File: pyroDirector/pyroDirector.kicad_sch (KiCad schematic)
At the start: 37 parts, among them J1 AudioJack3.5mm, J10 Ext_Btn_Down, J11 Ext_Btn_Up, J12 Ext_Btn_Left, J13 Ext_Btn_Right, J14 Ext_Btn_OK, J15 PWR_CONN, J16 CALIB_MODULE, J17 DISP_I2C, J2 Header_A1-A15, J3 Header_D14-19, J4 Header_D48-53, J5 V_Batt, J6 Header_ISP, J7 PWR_SWITCH, J8 Batt, J9 Ext_Btn_Cncl, Q1 MMBT2222A 1P, SW1 EN_SW, U1 MEGA_PRO_ATMEGA2560

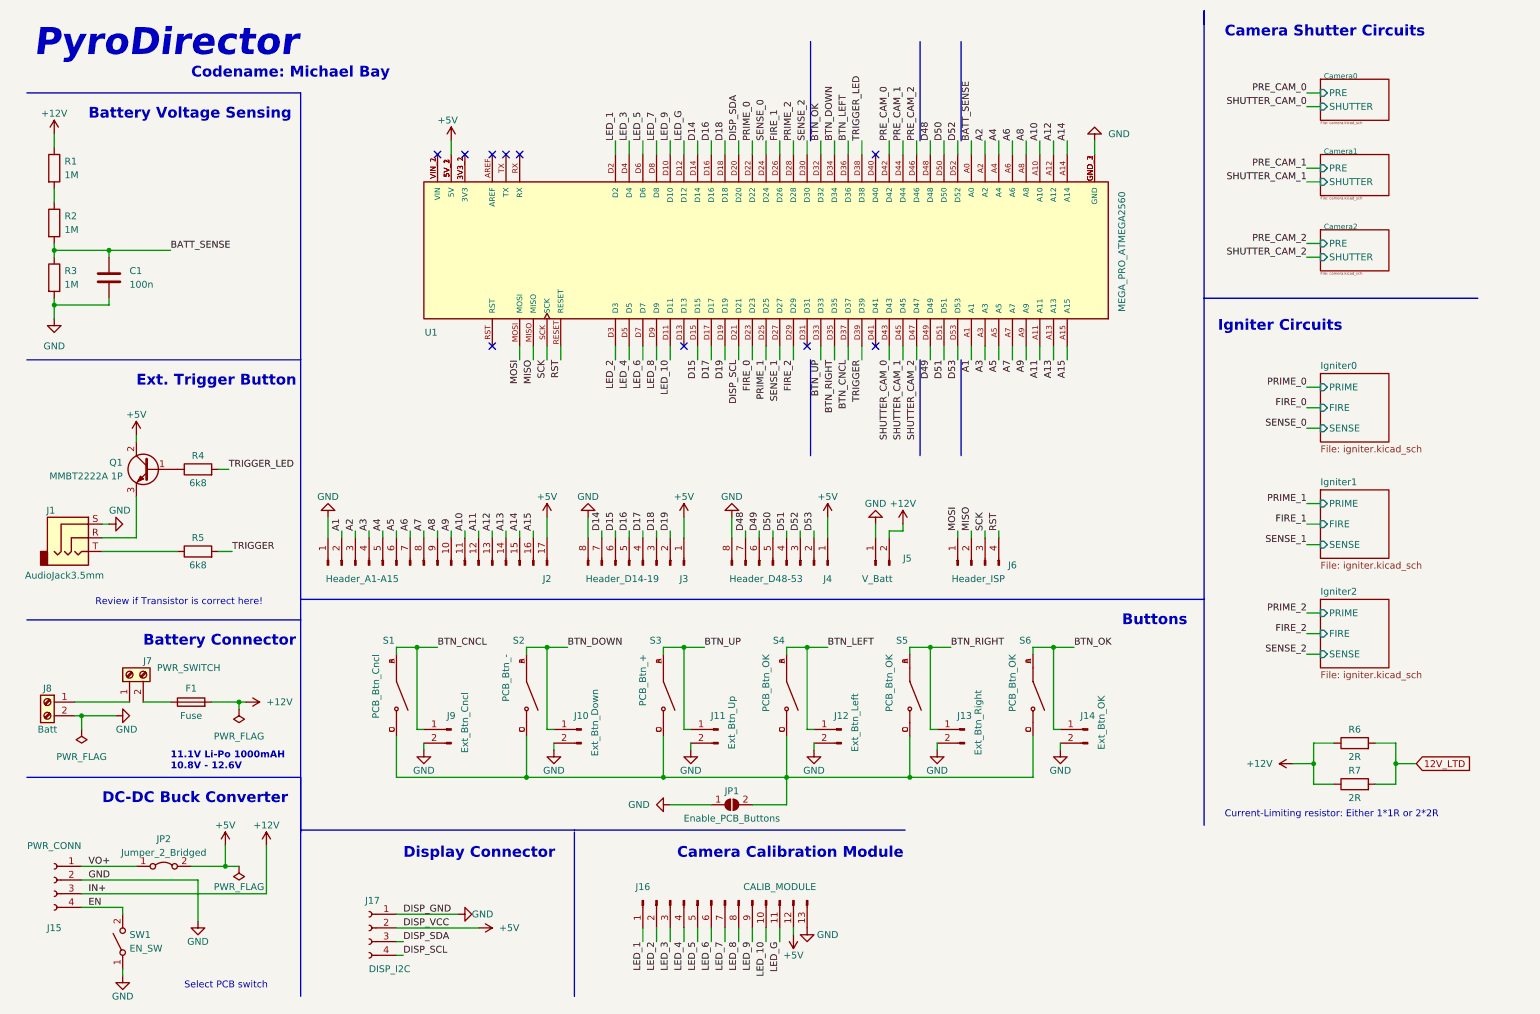
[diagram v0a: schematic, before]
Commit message: Added jacks and PCB switch
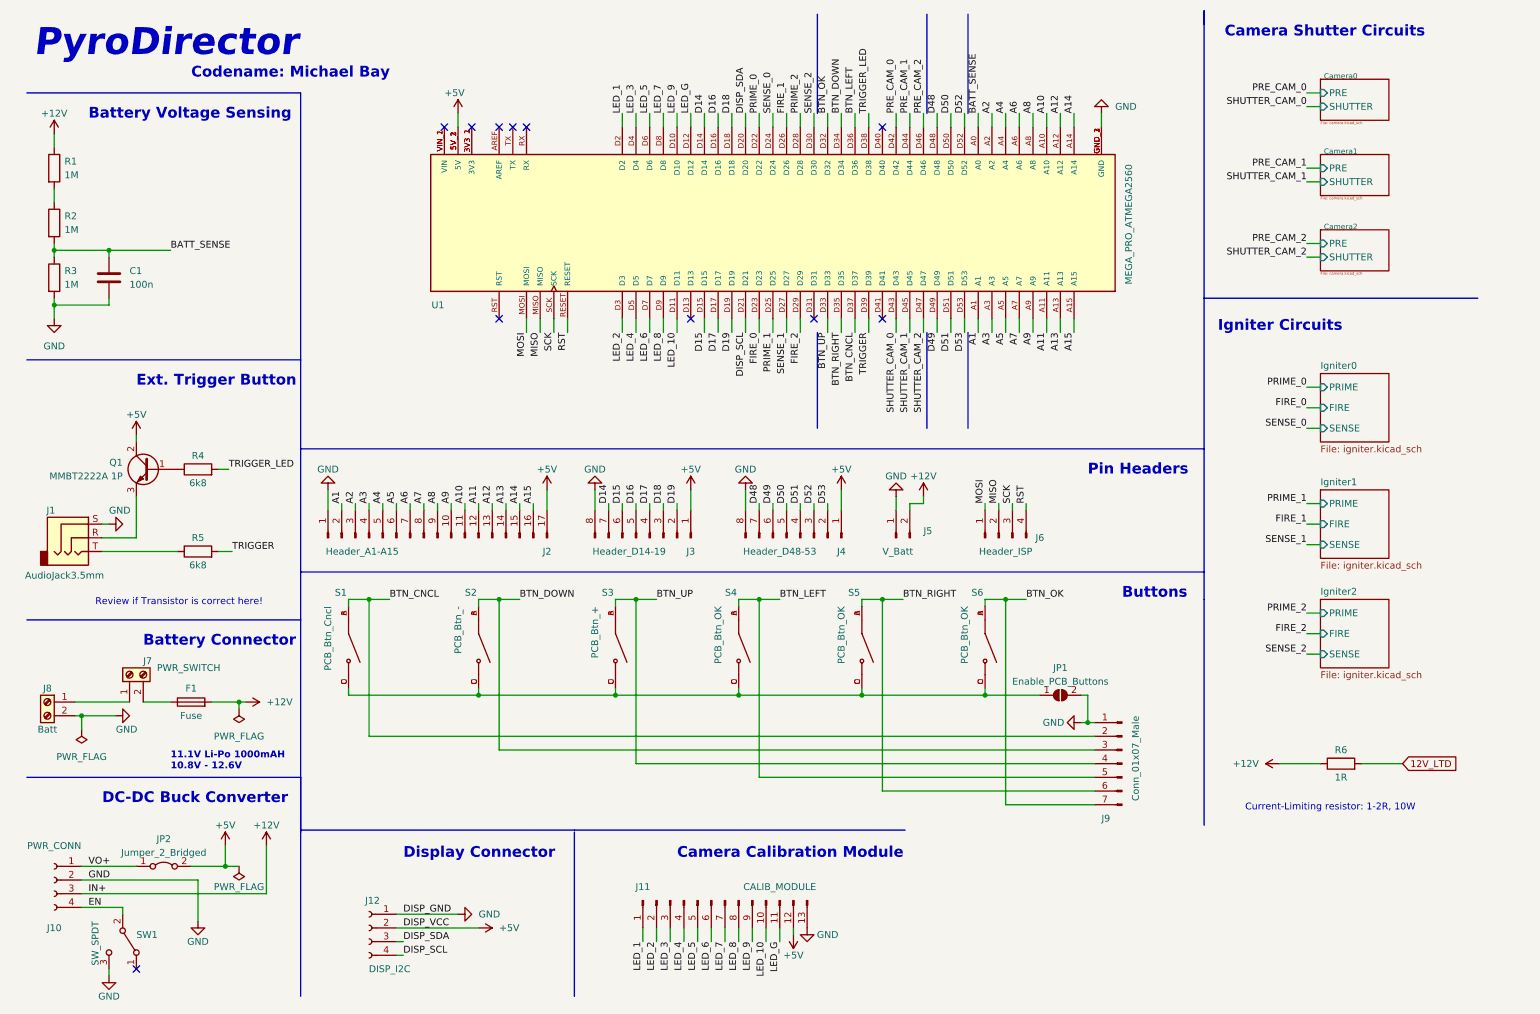
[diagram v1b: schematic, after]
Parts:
- removed J10: Ext_Btn_Down, symbol Connector:Conn_01x02_Male
- removed J11: Ext_Btn_Up, symbol Connector:Conn_01x02_Male
- removed J12: Ext_Btn_Left, symbol Connector:Conn_01x02_Male
- removed J13: Ext_Btn_Right, symbol Connector:Conn_01x02_Male
- removed J14: Ext_Btn_OK, symbol Connector:Conn_01x02_Male
- removed J9: Ext_Btn_Cncl, symbol Connector:Conn_01x02_Male
- removed R7: 2R, symbol Device:R
- removed SW1: EN_SW, symbol Switch:SW_SPST
- added J9: Conn_01x07_Male, symbol Connector:Conn_01x07_Male
- added SW1: SW_SPDT, custom_footprints:Saleforce_T80-S_TS-13_Slide_Switch, symbol Switch:SW_SPDT
- C1: footprint (none) -> Capacitor_SMD:C_0805_2012Metric_Pad1.18x1.45mm_HandSolder
- F1: footprint (none) -> custom_footprints:Fuseholder_Cylinder-5x20mm_Wuerth_WR-FSH
- J1: footprint (none) -> Connector_Audio:Jack_3.5mm_CUI_SJ1-3535NG_Horizontal
- J2: footprint (none) -> Connector_PinHeader_2.54mm:PinHeader_1x14_P2.54mm_Vertical
- J3, J4: footprint (none) -> Connector_PinHeader_2.54mm:PinHeader_1x05_P2.54mm_Vertical
- J5: footprint (none) -> Connector_PinHeader_2.54mm:PinHeader_1x01_P2.54mm_Vertical
- J6: footprint (none) -> Connector_PinHeader_2.54mm:PinHeader_1x04_P2.54mm_Vertical
- J7: footprint (none) -> TerminalBlock_Phoenix:TerminalBlock_Phoenix_MKDS-1,5-2_1x02_P5.00mm_Horizontal
- R6: value 2R -> 1R
- renumbered J15 to J10, J16 to J11, J17 to J12
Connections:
- net BTN_CNCL: now also J9.2 (Pin_2)
- net BTN_DOWN: now also J9.3 (Pin_3)
- net BTN_LEFT: now also J9.5 (Pin_5)
- net BTN_OK: now also J9.7 (Pin_7)
- net BTN_RIGHT: now also J9.6 (Pin_6)
- net BTN_UP: now also J9.4 (Pin_4)
- net EN: now also SW1.2 (B)
- net GND: now also JP1.2 (B), J9.1 (Pin_1), SW1.3 (C); no longer JP1.1 (A)
- net at S1.C, S1.D, S2.C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: now also JP1.1 (A); no longer JP1.2 (B)
- no-connect marks 10 -> 11
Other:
- note added: "Current-Limiting resistor: 1-2R, 10W"
- note added: "Pin Headers"
- note removed: "Current-Limiting resistor: Either 1*1R or 2*2R"
- note removed: "Select PCB switch"
- moved on the sheet: J2, J3, J4, J5, J6, JP1, R6, S1, S2, S3, S4, S5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

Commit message: first component placement, trigger header is missing!
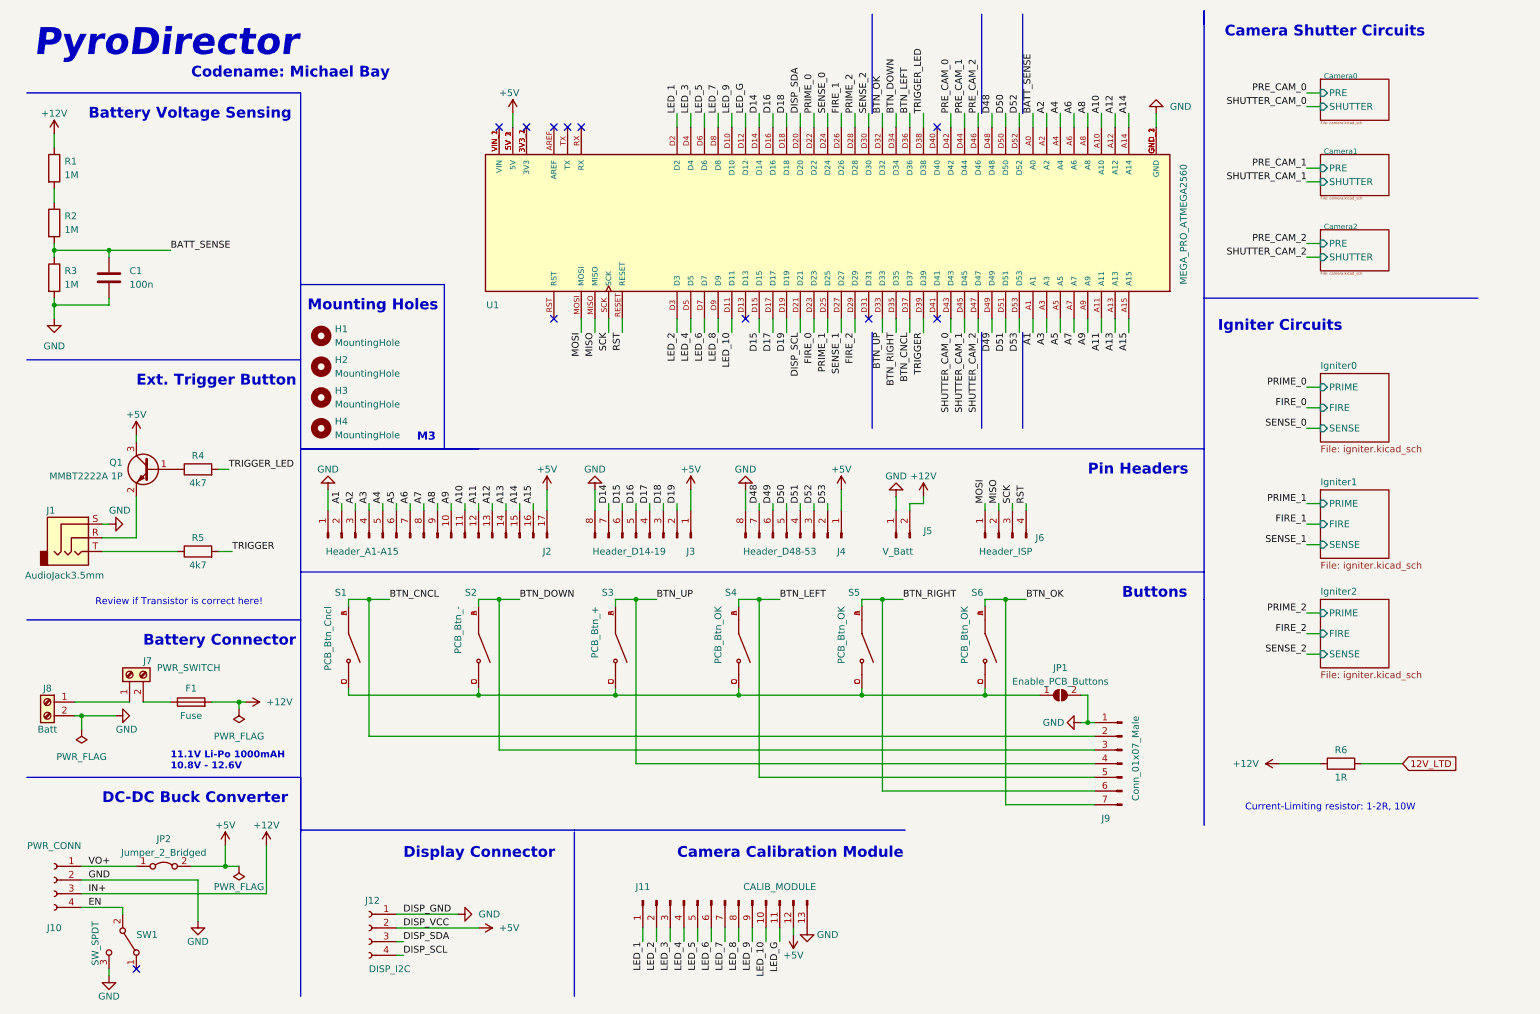
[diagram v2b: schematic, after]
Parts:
- removed Q1: MMBT2222A 1P, Package_TO_SOT_SMD:SOT-89-3, symbol Transistor_BJT:BCX56
- added H1, H2, H3, H4: MountingHole, MountingHole:MountingHole_3.2mm_M3, symbol Mechanical:MountingHole
- added Q1: MMBT2222A 1P, Package_TO_SOT_SMD:SOT-23, symbol JLCPCB_Parts:MMBT2222A 1P
- J10, J12: footprint (none) -> Connector_PinHeader_2.54mm:PinHeader_1x04_P2.54mm_Vertical
- J5: footprint Connector_PinHeader_2.54mm:PinHeader_1x01_P2.54mm_Vertical -> Connector_PinHeader_2.54mm:PinHeader_1x02_P2.54mm_Vertical
- J7: footprint TerminalBlock_Phoenix:TerminalBlock_Phoenix_MKDS-1,5-2_1x02_P5.00mm_Horizontal -> TerminalBlock_Phoenix:TerminalBlock_Phoenix_PT-1,5-2-5.0-H_1x02_P5.00mm_Horizontal
- J8: footprint (none) -> TerminalBlock_Phoenix:TerminalBlock_Phoenix_PT-1,5-2-5.0-H_1x02_P5.00mm_Horizontal
- J9: footprint (none) -> Connector_PinHeader_2.54mm:PinHeader_1x07_P2.54mm_Vertical
- JP2: footprint (none) -> TestPoint:TestPoint_Bridge_Pitch2.54mm_Drill1.0mm
- R1, R2, R3: footprint (none) -> Resistor_SMD:R_0805_2012Metric_Pad1.20x1.40mm_HandSolder
- R4, R5: value 6k8 -> 4k7; footprint (none) -> Resistor_SMD:R_0805_2012Metric_Pad1.20x1.40mm_HandSolder
- R6: footprint (none) -> custom_footprints:R_Axial_Power_L48.0mm_W10mm_P55.88mm
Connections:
- net +5V: now also Q1.3 (C)
- net at R4.1: now also Q1.1 (B)
- net at J1.R: now also Q1.2 (E)
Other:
- note added: "M3"
- note added: "Mounting Holes"
- moved on the sheet: U1

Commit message: placement improvements, added missing header -->should we use handsolder pads?
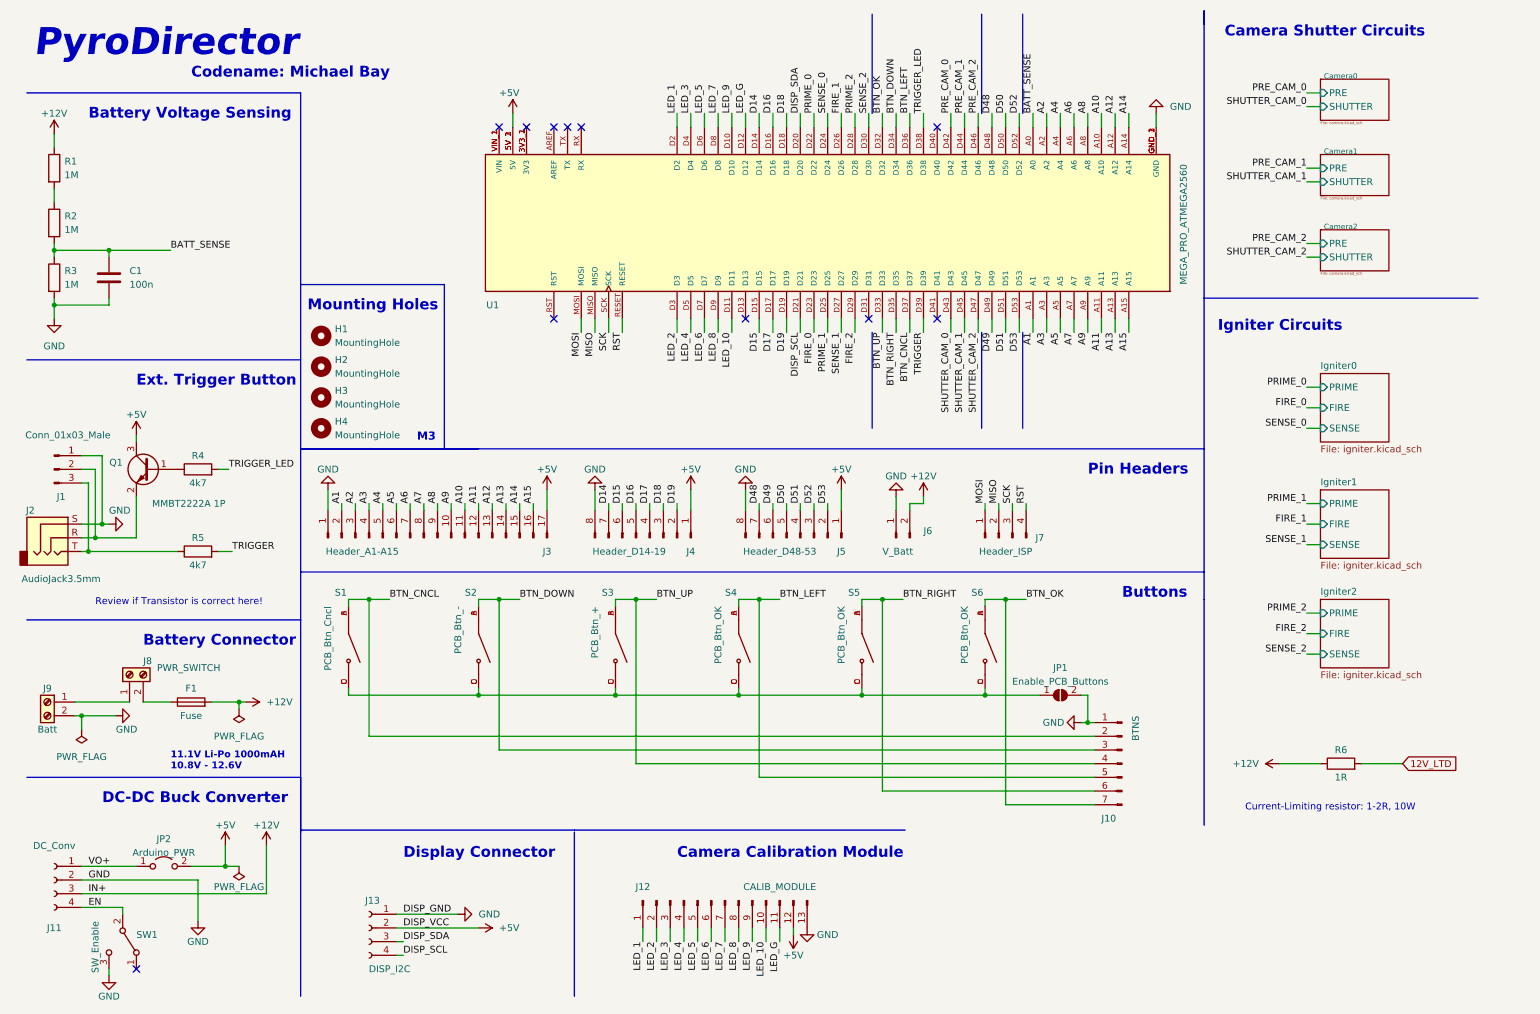
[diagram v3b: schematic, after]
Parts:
- added J1: Conn_01x03_Male, Connector_PinHeader_2.54mm:PinHeader_1x03_P2.54mm_Vertical, symbol Connector:Conn_01x03_Male
- J10: renamed from J9; value Conn_01x07_Male -> BTNS
- J11: renamed from J10; value PWR_CONN -> DC_Conv
- J3: renamed from J2; footprint Connector_PinHeader_2.54mm:PinHeader_1x14_P2.54mm_Vertical -> Connector_PinHeader_2.54mm:PinHeader_1x17_P2.54mm_Vertical
- J4: renamed from J3; footprint Connector_PinHeader_2.54mm:PinHeader_1x05_P2.54mm_Vertical -> Connector_PinHeader_2.54mm:PinHeader_1x08_P2.54mm_Vertical
- J5: renamed from J4; footprint Connector_PinHeader_2.54mm:PinHeader_1x05_P2.54mm_Vertical -> Connector_PinHeader_2.54mm:PinHeader_1x08_P2.54mm_Vertical
- JP2: value Jumper_2_Bridged -> Arduino_PWR; symbol Jumper:Jumper_2_Bridged -> Jumper:Jumper_2_Open
- SW1: value SW_SPDT -> SW_Enable
- renumbered J11 to J12, J12 to J13, J1 to J2, J5 to J6, J6 to J7, J7 to J8, J8 to J9
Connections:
- net GND: now also J1.1 (Pin_1)
- net at J2.T, R5.1: now also J1.3 (Pin_3)
- net at J2.R, Q1.2 (E): now also J1.2 (Pin_2)
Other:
- moved on the sheet: J2

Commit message: placement & 3-D models complete
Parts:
- removed J5: Header_D48-53, Connector_PinHeader_2.54mm:PinHeader_1x08_P2.54mm_Vertical, symbol Connector:Conn_01x08_Male
- J4: value Header_D14-19 -> Header_D14-19_D49_51_53; footprint Connector_PinHeader_2.54mm:PinHeader_1x08_P2.54mm_Vertical -> Connector_PinHeader_2.54mm:PinHeader_1x11_P2.54mm_Vertical; symbol Connector:Conn_01x08_Male -> Connector:Conn_01x11_Male
- JP2: footprint TestPoint:TestPoint_Bridge_Pitch2.54mm_Drill1.0mm -> Connector_PinHeader_2.54mm:PinHeader_1x02_P2.54mm_Vertical
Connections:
- net D48 is gone; now on net SENSE_2: U1.D48
- net D50 is gone; now on net PRIME_2: U1.D50
- net D52 is gone; now on net FIRE_1: U1.D52
- net BTN_CNCL: now also U1.D45; no longer U1.D37
- net BTN_DOWN: now also U1.D42; no longer U1.D34
- net BTN_LEFT: now also U1.D44; no longer U1.D36
- net BTN_OK: now also U1.D40; no longer U1.D32
- net BTN_RIGHT: now also U1.D43; no longer U1.D35
- net BTN_UP: now also U1.D41; no longer U1.D33
- net D14: now also J4.10 (Pin_10); no longer J4.7 (Pin_7)
- net D15: now also J4.9 (Pin_9); no longer J4.6 (Pin_6)
- net D16: now also J4.8 (Pin_8); no longer J4.5 (Pin_5)
- net D17: now also J4.7 (Pin_7); no longer J4.4 (Pin_4)
- net D18: now also J4.6 (Pin_6); no longer J4.3 (Pin_3)
- net D19: now also J4.5 (Pin_5); no longer J4.2 (Pin_2)
- net D49: now also J4.4 (Pin_4)
- net D51: now also J4.3 (Pin_3)
- net D53: now also J4.2 (Pin_2)
- net FIRE_1: no longer U1.D26
- net GND: now also J4.11 (Pin_11); no longer J4.8 (Pin_8)
- net PRE_CAM_0: now also U1.D34; no longer U1.D42
- net PRE_CAM_1: now also U1.D36; no longer U1.D44
- net PRE_CAM_2: now also U1.D38; no longer U1.D46
- net PRIME_2: no longer U1.D28
- net SENSE_2: no longer U1.D30
- net SHUTTER_CAM_0: now also U1.D35; no longer U1.D43
- net SHUTTER_CAM_1: now also U1.D37; no longer U1.D45
- net SHUTTER_CAM_2: now also U1.D39; no longer U1.D47
- net TRIGGER: now also U1.D33; no longer U1.D39
- net TRIGGER_LED: now also U1.D32; no longer U1.D38
- no-connect marks 11 -> 14
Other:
- moved on the sheet: J6, J7

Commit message: layout in progress
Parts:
- H1, H2, H3, H4: footprint MountingHole:MountingHole_3.2mm_M3 -> MountingHole:MountingHole_3.2mm_M3_Pad_Via; symbol Mechanical:MountingHole -> Mechanical:MountingHole_Pad
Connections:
- net BTN_RIGHT: now also U1.D46; no longer U1.D43
- net FIRE_0: now also U1.D30; no longer U1.D23
- net FIRE_2: now also U1.D47; no longer U1.D29
- net GND: now also H1.1, H2.1, H3.1, H4.1
- net PRIME_0: now also U1.D31; no longer U1.D22
- net PRIME_1: now also U1.D28; no longer U1.D25
- net SENSE_0: now also U1.D23; no longer U1.D24
- net SENSE_1: now also U1.D26; no longer U1.D27
